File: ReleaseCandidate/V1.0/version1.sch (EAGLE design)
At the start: 70 parts, among them IC1 ADG1604D, IC2 LM317MBSTT3, IC3 AD8610MR, IC4 AD8610MR, IC5 337IMP, X1 PN61729-S, X2 BU-SMA-H

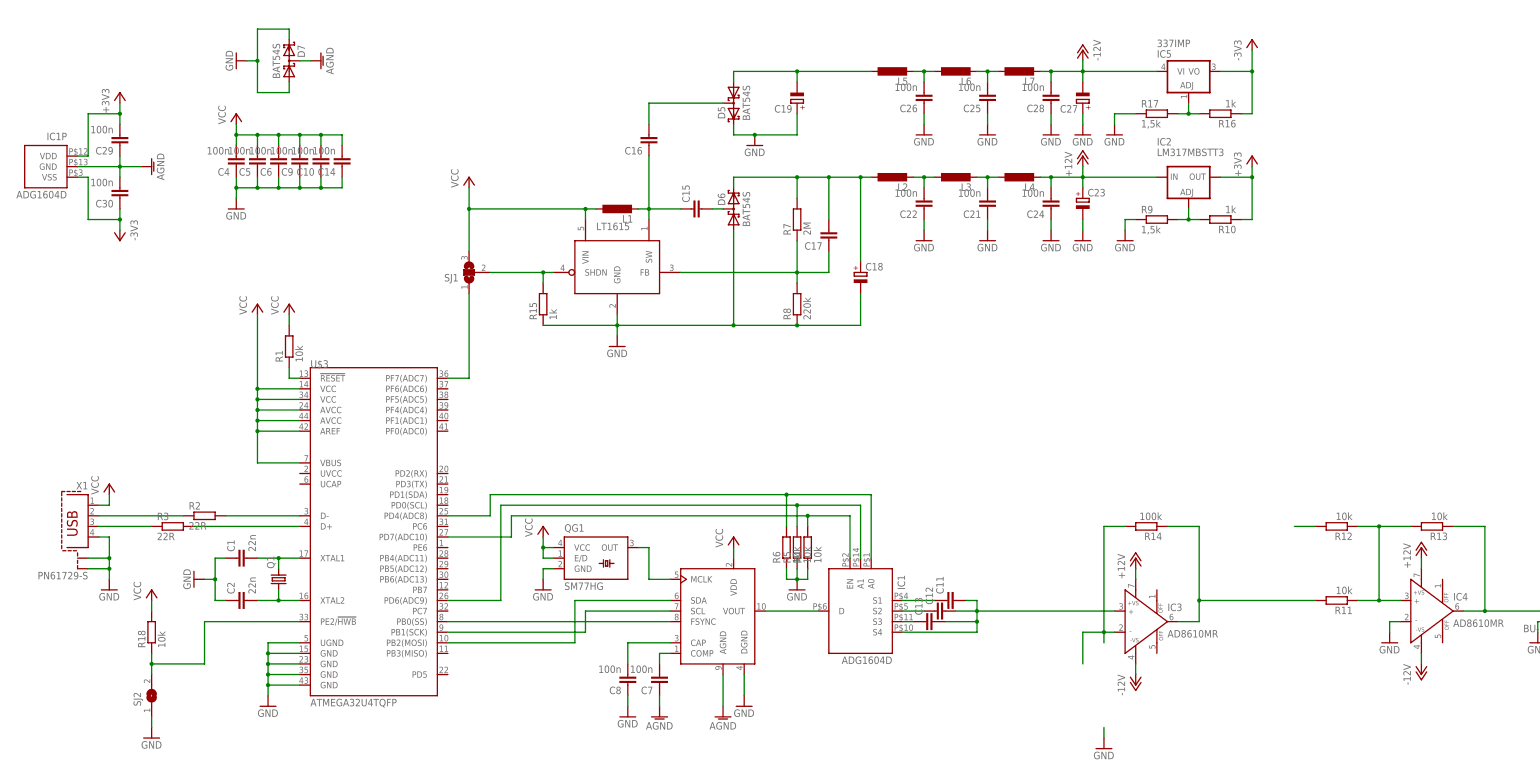
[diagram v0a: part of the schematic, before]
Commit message: finish circuit, create board
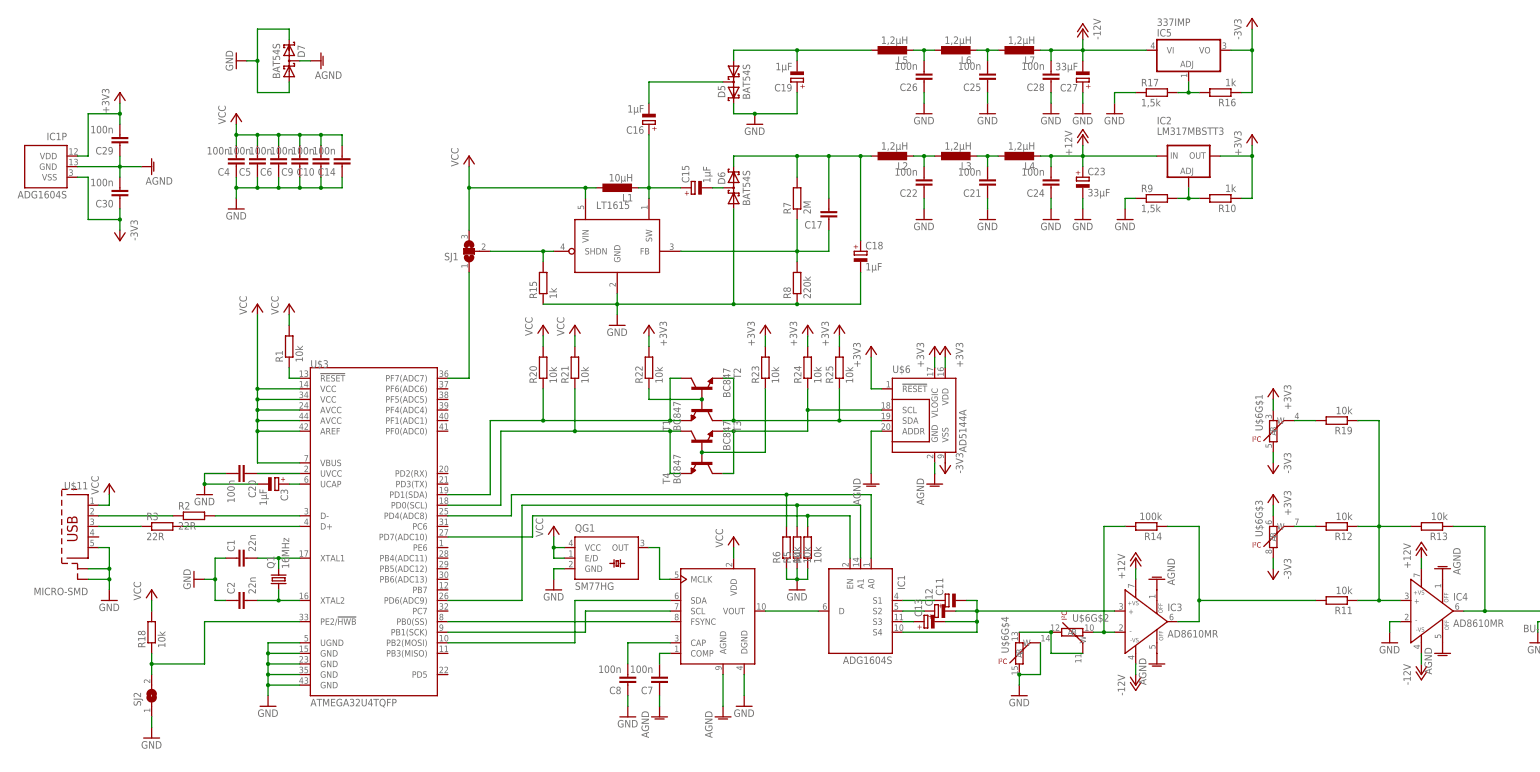
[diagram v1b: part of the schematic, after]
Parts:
- removed X1: PN61729-S, con-berg:PN61729-S
- added C20: 100n, rcl:C-EUC0603
- added C3: 1µF, rcl:CPOL-EUSMCA
- added R19, R20, R21, R22, R23, R24, R25: 10k, rcl:R-EU_R0603
- added T1, T2, T3, T4: BC847, transistor:BC847
- added U$11: MICRO-SMD, con-berg:MICRO-SMD
- added U$6: AD5144A, analog-devices:AD5144A
- C11, C12, C13: device rcl:C-EU025-024X044 -> rcl:CPOL-EUSMCB
- C15, C16: value (none) -> 1µF; device rcl:C-EU025-030X050 -> rcl:CPOL-EUSMCA
- C17: device rcl:C-EU025-030X050 -> rcl:C-EUC0603
- C18, C19: value (none) -> 1µF; device rcl:CPOL-EUE2,5-6E -> rcl:CPOL-EUSMCA
- C23, C27: value (none) -> 33µF; device rcl:CPOL-EUSMCA -> rcl:CPOL-EUSMCB
- IC1: value ADG1604D -> ADG1604S; device analog-devices:ADG1604D -> analog-devices:ADG1604S
- L1: value (none) -> 10µH; device rcl:L-EUL0805 -> rcl:L-EUL3015
- L2, L3, L4, L5, L6, L7: value (none) -> 1,2µH; device rcl:L-EUL0805 -> rcl:L-EU0805
- Q1: value (none) -> 16MHz
- R14, R7, R8: device rcl:R-EU_0207/10 -> rcl:R-EU_R0603
- U$1: value AD9833-P -> AD9833-SMD; device analog-devices:AD9833-P -> analog-devices:AD9833-SMD
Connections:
- new net N$42: R21.1, T3.E, T4.C, U$3.PD0(SCL)
- new net N$43: R20.1, T1.C, T2.E, U$3.PD1(SDA)
- new net N$44: U$6G$2.B, U$6G$2.W, U$6G$4.A
- new net N$45: R12.2, U$6G$3.W
- new net N$46: R22.1, T1.B, T2.B
- new net N$47: R23.1, T3.B, T4.B
- new net N$48: R24.1, T3.C, T4.E, U$6G$5.SCL
- new net N$49: R25.1, T1.E, T2.C, U$6G$5.SDA
- new net N$52: C3.+, U$3.UCAP
- new net N$53: C20.1, U$3.UVCC
- net +3V3: now also R22.2, R23.2, R24.2, R25.2, U$6G$1.A, U$6G$3.A, U$6G$5.!RESET, U$6G$5.VDD, U$6G$5.VLOGIC
- net -3V3: now also U$6G$1.B, U$6G$3.B, U$6G$5.VSS
- net AGND: now also IC3.OFF@1, IC3.OFF@2, IC4.OFF@1, IC4.OFF@2, U$6G$5.ADDR, U$6G$5.GND
- net GND: now also C20.2, C3.-, U$11.5, U$11.S1, U$11.S2, U$6G$4.B, U$6G$4.W; no longer X1.4, X1.S1, X1.S2
- net N$13: now also U$11.3; no longer X1.3
- net N$14: now also U$11.2; no longer X1.2
- net N$17: now also C13.+; no longer C13.1
- net N$18: now also C12.+; no longer C12.1
- net N$19: now also C11.+; no longer C11.1
- net N$20: now also C11.-, C12.-, C13.-; no longer C11.2, C12.2, C13.2
- net N$24: now also C16.-; no longer C16.2
- net N$25: now also C15.+, C16.+; no longer C15.1, C16.1
- net N$3: now also C15.-; no longer C15.2
- net N$32: now also R19.1
- net N$33: now also R19.2, U$6G$1.W; no longer R12.2
- net N$34: now also U$6G$2.A
- net VCC: now also R20.2, R21.2, U$11.1; no longer X1.1
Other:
- moved on the sheet: C17, C18, C19, C21, C22, C23, C24, C25, C26, C27, C28, D5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

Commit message: first steps on the board, add scematic picture
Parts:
- C1, C2: device rcl:C-EUC1206 -> rcl:C-EUC0603
- SJ2: device jumper:SJW -> jumper:SJ
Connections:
- net AGND: now also X2.2
- net GND: no longer X2.2
- net N$25: now also C15.-; no longer C15.+
- net N$3: now also C15.+; no longer C15.-
- net N$39: now also U$3.PE6; no longer U$3.PF7(ADC7)
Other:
- note added: "©2015 Hendrik Lüth | LabConnect | Signalgenerator | https://github.com/labconnect"
- moved on the sheet: C10, C11, C12, C14, C15, C29, C30, C4, C5, C6, C9, D7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

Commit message: finish layout
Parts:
- added C31, C32, C33, C34: 100n, rcl:C-EUC0603
- added LED1: (no value), led:LEDCHIP-LED0603
- added PAD1, PAD2, PAD3, PAD4: WIREPADSMD1,27-254, wirepad:WIREPADSMD1,27-254
- added R26: 150, rcl:R-EU_R0603
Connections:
- new net N$50: PAD2.P, U$3.PB3(MISO)
- new net N$51: LED1.A, R26.1
- net +12V: now also C31.2, C33.2
- net -12V: now also C32.1, C34.1
- net AGND: now also C31.1, C32.2, C33.1, C34.2, IC4.IN+, U$6G$4.B, U$6G$4.W
- net GND: now also LED1.C; no longer IC4.IN-, U$6G$4.B, U$6G$4.W
- net N$32: now also IC4.IN-; no longer IC4.IN+
- net N$4: now also PAD3.P
- net N$8: now also PAD1.P
- net N$9: now also PAD4.P
- net VCC: now also R26.2
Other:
- moved on the sheet: IC4, X2
